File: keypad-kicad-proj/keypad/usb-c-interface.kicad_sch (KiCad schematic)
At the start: 23 parts, among them J2 USB4105-GF-A, Q1 BC817, Q2 BC817, U3 CP2102N-A01-GQFN24

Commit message: battery source
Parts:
- added C9: 1uF, symbol PutRocketLab_RCL:C_Small
- added SW13: SW_SPST, symbol Switch:SW_SPST
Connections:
- net GND: now also C9.2, SW13.1 (A)
- net RTS: now also C9.1, SW13.2 (B)
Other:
- note added: "Manual reset"
- moved on the sheet: C4, D18, D19, D20, D21, J2

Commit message: rest of the schematic
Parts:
- removed C9: 1uF, symbol PutRocketLab_RCL:C_Small
- removed SW13: SW_SPST, symbol Switch:SW_SPST
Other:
- note removed: "Manual reset"
- title: (none) -> Keypad board
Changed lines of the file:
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@@
 (kicad_sch (version 20230121) (generator eeschema)
   (paper "A4")
+  (title_block
+    (title "Keypad board")
+    (date "2023-11-15")
+    (rev "1.1")
+  )
   (junction (at 214.63 118.11) (diameter 0) (color 0 0 0 0)
   )
@@
   (junction (at 77.47 55.88) (diameter 0) (color 0 0 0 0)
   )
-  (junction (at 257.81 142.24) (diameter 0) (color 0 0 0 0)
-  )
   (junction (at 90.17 154.94) (diameter 0) (color 0 0 0 0)
   )
@@
   )
   (junction (at 165.1 111.76) (diameter 0) (color 0 0 0 0)
-  )
-  (junction (at 265.43 133.35) (diameter 0) (color 0 0 0 0)
   )
   (junction (at 78.74 154.94) (diameter 0) (color 0 0 0 0)
@@
     (stroke (width 0) (type default))
   )
-  (wire (pts (xy 257.81 142.24) (xy 265.43 142.24))
-    (stroke (width 0) (type default))
-  )
   (wire (pts (xy 102.87 45.72) (xy 109.22 45.72))
     (stroke (width 0) (type default))
@@
     (stroke (width 0) (type default))
   )
-  (wire (pts (xy 265.43 133.35) (xy 265.43 135.89))
-    (stroke (width 0) (type default))
-  )
   (wire (pts (xy 267.97 77.47) (xy 262.89 77.47))
     (stroke (width 0) (type default))
@@
     (stroke (width 0) (type default))
   )
-  (wire (pts (xy 250.19 142.24) (xy 257.81 142.24))
-    (stroke (width 0) (type default))
-  )
   (wire (pts (xy 76.2 185.42) (xy 76.2 152.4))
     (stroke (width 0) (type default))
@@
     (stroke (width 0) (type default))
   )
-  (wire (pts (xy 262.89 133.35) (xy 265.43 133.35))
-    (stroke (width 0) (type default))
-  )
   (wire (pts (xy 72.39 175.26) (xy 72.39 176.53))
     (stroke (width 0) (type default))
@@
     (stroke (width 0) (type default))
   )
-  (wire (pts (xy 257.81 144.78) (xy 257.81 142.24))
-    (stroke (width 0) (type default))
-  )
   (wire (pts (xy 170.18 101.6) (xy 198.12 101.6))
     (stroke (width 0) (type default))
@@
     (stroke (width 0) (type default))
   )
-  (wire (pts (xy 252.73 133.35) (xy 250.19 133.35))
-    (stroke (width 0) (type default))
-  )
   (wire (pts (xy 26.67 157.48) (xy 29.21 157.48))
     (stroke (width 0) (type default))
@@
     (stroke (width 0) (type default))
   )
-  (wire (pts (xy 265.43 133.35) (xy 267.97 133.35))
-    (stroke (width 0) (type default))
-  )
   (wire (pts (xy 196.85 106.68) (xy 198.12 106.68))
     (stroke (width 0) (type default))
@@
     (stroke (width 0) (type default))
   )
-  (wire (pts (xy 265.43 142.24) (xy 265.43 140.97))
-    (stroke (width 0) (type default))
-  )
   (wire (pts (xy 139.7 160.02) (xy 135.89 160.02))
     (stroke (width 0) (type default))
   )
   (wire (pts (xy 77.47 48.26) (xy 74.93 48.26))
-    (stroke (width 0) (type default))
-  )
-  (wire (pts (xy 250.19 133.35) (xy 250.19 142.24))
     (stroke (width 0) (type default))
   )
@@
   (text "USB-C (UART)" (at 36.83 22.86 0)
     (effects (font (size 3 3) (thickness 0.6) bold) (justify left bottom))
-  )
-  (text "Manual reset" (at 250.19 123.19 0)
-    (effects (font (size 1.5 1.5) (thickness 0.6) bold) (justify left bottom))
-  )
-  (global_label "RTS" (shape output) (at 267.97 133.35 0) (fields_autoplaced)
-    (effects (font (size 1.27 1.27)) (justify left))
-    (property "Intersheetrefs" "${INTERSHEET_REFS}" (at 274.4023 133.35 0)
-      (effects (font (size 1.27 1.27)) (justify left) hide)
-    )
   )
   (global_label "UART_RX" (shape input) (at 229.87 86.36 0) (fields_autoplaced)
@@
     )
   )
-  (symbol (lib_id "PutRocketLab_RCL:C_Small") (at 265.43 138.43 0) (unit 1)
-    (in_bom yes) (on_board yes) (dnp no) (fields_autoplaced)
-    (property "Reference" "C9" (at 267.97 137.1663 0)
-      (effects (font (size 1.27 1.27)) (justify left))
-    )
-    (property "Value" "1uF" (at 267.97 139.7063 0)
-      (effects (font (size 1.27 1.27)) (justify left))
-    )
-    (property "Footprint" "" (at 265.43 138.43 0)
-      (effects (font (size 1.27 1.27)) hide)
-    )
-    (property "Datasheet" "~" (at 265.43 138.43 0)
-      (effects (font (size 1.27 1.27)) hide)
-    )
-    (pin "1")
-    (pin "2")
-    (instances
-      (project "keypad"
-        (path "/26078c39-1d91-4154-8719-da74cb453e74/8c59234c-4b92-497c-9a92-28fee1185425"
-          (reference "C9") (unit 1)
-        )
-      )
-    )
-  )
   (symbol (lib_id "PutRocketLab_RCL:C_Small") (at 139.7 154.94 0) (unit 1)
     (in_bom yes) (on_board yes) (dnp no) (fields_autoplaced)
@@
         (path "/26078c39-1d91-4154-8719-da74cb453e74/8c59234c-4b92-497c-9a92-28fee1185425"
           (reference "R8") (unit 1)
-        )
-      )
-    )
-  )
-  (symbol (lib_id "Switch:SW_SPST") (at 257.81 133.35 0) (unit 1)
-    (in_bom yes) (on_board yes) (dnp no) (fields_autoplaced)
-    (property "Reference" "SW13" (at 257.81 127 0)
-      (effects (font (size 1.27 1.27)))
-    )
-    (property "Value" "SW_SPST" (at 257.81 129.54 0)
-      (effects (font (size 1.27 1.27)))
-    )
-    (property "Footprint" "" (at 257.81 133.35 0)
-      (effects (font (size 1.27 1.27)) hide)
-    )
-    (property "Datasheet" "~" (at 257.81 133.35 0)
-      (effects (font (size 1.27 1.27)) hide)
-    )
-    (pin "1")
-    (pin "2")
-    (instances
-      (project "keypad"
-        (path "/26078c39-1d91-4154-8719-da74cb453e74/4b0bf287-ff22-46d2-9a21-8f5bc40c75ad"
-          (reference "SW13") (unit 1)
-        )
-        (path "/26078c39-1d91-4154-8719-da74cb453e74/8c59234c-4b92-497c-9a92-28fee1185425"
-          (reference "SW25") (unit 1)
         )
       )
@@
         )
       )
-    )
-  )
-  (symbol (lib_id "PUT_RocketLab_power:GND") (at 257.81 144.78 0) (unit 1)
-    (in_bom yes) (on_board yes) (dnp no) (fields_autoplaced)
-    (property "Reference" "#PWR014" (at 257.81 151.13 0)
-      (effects (font (size 1.27 1.27)) hide)
-    )
-    (property "Value" "GND" (at 257.81 149.86 0)
-      (effects (font (size 1.27 1.27)))
-    )
-    (property "Footprint" "" (at 257.81 144.78 0)
-      (effects (font (size 1.27 1.27)) hide)
-    )
-    (property "Datasheet" "" (at 257.81 144.78 0)
-      (effects (font (size 1.27 1.27)) hide)
-    )
-    (pin "1")
-    (instances
-      (project "keypad"
-        (path "/26078c39-1d91-4154-8719-da74cb453e74"
-          (reference "#PWR014") (unit 1)
-        )
-        (path "/26078c39-1d91-4154-8719-da74cb453e74/8c59234c-4b92-497c-9a92-28fee1185425"
-          (reference "#PWR042") (unit 1)
-        )
-      )

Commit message: footprints
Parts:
- C3, C4, C6: footprint (none) -> Capacitor_SMD:C_0402_1005Metric
- C5: footprint (none) -> Capacitor_SMD:C_0603_1608Metric
- R10, R11, R7, R8, R9: footprint (none) -> Resistor_SMD:R_0603_1608Metric
- R5: footprint (none) -> Resistor_SMD:R_0402_1005Metric
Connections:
- net +3V3: now also U3.5 (VIO)
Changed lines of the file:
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@@
   (junction (at 245.11 93.98) (diameter 0) (color 0 0 0 0)
+  )
+  (junction (at 210.82 69.85) (diameter 0) (color 0 0 0 0)
   )
   (junction (at 170.18 101.6) (diameter 0) (color 0 0 0 0)
@@
     (stroke (width 0) (type default))
   )
+  (wire (pts (xy 213.36 69.85) (xy 210.82 69.85))
+    (stroke (width 0) (type default))
+  )
   (wire (pts (xy 26.67 73.66) (xy 81.28 73.66))
     (stroke (width 0) (type default))
@@
   )
   (wire (pts (xy 31.75 45.72) (xy 34.29 45.72))
+    (stroke (width 0) (type default))
+  )
+  (wire (pts (xy 213.36 71.12) (xy 213.36 69.85))
     (stroke (width 0) (type default))
   )
@@
       (effects (font (size 1.27 1.27)) (justify left))
     )
-    (property "Footprint" "" (at 64.77 99.06 0)
+    (property "Footprint" "Capacitor_SMD:C_0402_1005Metric" (at 64.77 99.06 0)
       (effects (font (size 1.27 1.27)) hide)
     )
@@
       (effects (font (size 1.27 1.27)) (justify right))
     )
-    (property "Footprint" "" (at 160.02 96.52 0)
+    (property "Footprint" "Resistor_SMD:R_0402_1005Metric" (at 160.02 96.52 0)
       (effects (font (size 1.27 1.27)) hide)
     )
@@
       (effects (font (size 1.27 1.27)) (justify left))
     )
-    (property "Footprint" "" (at 170.18 106.68 0)
+    (property "Footprint" "Capacitor_SMD:C_0603_1608Metric" (at 170.18 106.68 0)
       (effects (font (size 1.27 1.27)) hide)
     )
@@
       (effects (font (size 1.27 1.27)) (justify left))
     )
-    (property "Footprint" "" (at 139.7 154.94 0)
+    (property "Footprint" "Capacitor_SMD:C_0402_1005Metric" (at 139.7 154.94 0)
       (effects (font (size 1.27 1.27)) hide)
     )
@@
       (effects (font (size 1.27 1.27)) (justify left))
     )
-    (property "Footprint" "" (at 191.77 88.9 0)
+    (property "Footprint" "Resistor_SMD:R_0603_1608Metric" (at 191.77 88.9 0)
       (effects (font (size 1.27 1.27)) hide)
     )
@@
       (effects (font (size 1.27 1.27)) (justify right))
     )
-    (property "Footprint" "" (at 160.02 106.68 0)
+    (property "Footprint" "Resistor_SMD:R_0603_1608Metric" (at 160.02 106.68 0)
       (effects (font (size 1.27 1.27)) hide)
     )
@@
       (effects (font (size 1.27 1.27)))
     )
-    (property "Footprint" "" (at 191.77 69.85 0)
+    (property "Footprint" "Capacitor_SMD:C_0402_1005Metric" (at 191.77 69.85 0)
       (effects (font (size 1.27 1.27)) hide)
     )
@@
       (effects (font (size 1.27 1.27)) (justify right))
     )
-    (property "Footprint" "" (at 191.77 78.74 0)
+    (property "Footprint" "Resistor_SMD:R_0603_1608Metric" (at 191.77 78.74 0)
       (effects (font (size 1.27 1.27)) hide)
     )
@@
       (effects (font (size 1.27 1.27)) (justify right))
     )
-    (property "Footprint" "" (at 251.46 83.82 0)
+    (property "Footprint" "Resistor_SMD:R_0603_1608Metric" (at 251.46 83.82 0)
       (effects (font (size 1.27 1.27)) hide)
     )
@@
       (effects (font (size 1.27 1.27)) (justify right))
     )
-    (property "Footprint" "" (at 251.46 100.33 0)
-      (effects (font (size 1.27 1.27)) hide)
-    )
+    (property "Footprint" "Resistor_SMD:R_0603_1608Metric" (at 251.46 100.33 0)
+      (effects (font (size 1.27 1.27)) hide)
+    )

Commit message: add all footprints & move libs to project specific
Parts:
- D17, D18: footprint (none) -> Diode_SMD:D_2114_3652Metric
- J2: footprint PUTRocketLab_other:GCT_USB4105-GF-A -> PUT_RocketLab_other:GCT_USB4105-GF-A
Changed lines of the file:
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@@
       (effects (font (size 1.27 1.27)))
     )
-    (property "Footprint" "PUTRocketLab_other:GCT_USB4105-GF-A" (at 54.61 45.72 0)
+    (property "Footprint" "PUT_RocketLab_other:GCT_USB4105-GF-A" (at 54.61 45.72 0)
       (effects (font (size 1.27 1.27)) (justify left bottom) hide)
     )
@@
       (effects (font (size 1.27 1.27)))
     )
-    (property "Footprint" "" (at 125.73 147.32 0)
-      (effects (font (size 1.27 1.27)) hide)
-    )
-    (property "Datasheet" "~" (at 125.73 147.32 0)
+    (property "Footprint" "Diode_SMD:D_2114_3652Metric" (at 125.73 147.32 0)
+      (effects (font (size 1.27 1.27)) hide)
+    )
+    (property "Datasheet" "https://www.mouser.pl/datasheet/2/80/CDBA240LR_HF_Thru514819__CDBA2200LR_HF_RevB-2505020.pdf" (at 125.73 147.32 0)
       (effects (font (size 1.27 1.27)) hide)
     )
@@
       (effects (font (size 1.27 1.27)))
     )
-    (property "Footprint" "PUTRocketLab_other:GCT_USB4105-GF-A" (at 49.53 157.48 0)
+    (property "Footprint" "PUT_RocketLab_other:GCT_USB4105-GF-A" (at 49.53 157.48 0)
       (effects (font (size 1.27 1.27)) (justify left bottom) hide)
     )
@@
       (effects (font (size 1.27 1.27)))
     )
-    (property "Footprint" "" (at 50.8 91.44 0)
-      (effects (font (size 1.27 1.27)) hide)
-    )
-    (property "Datasheet" "~" (at 50.8 91.44 0)
-      (effects (font (size 1.27 1.27)) hide)
-    )
+    (property "Footprint" "Diode_SMD:D_2114_3652Metric" (at 50.8 91.44 0)
+      (effects (font (size 1.27 1.27)) hide)
+    )
+    (property "Datasheet" "https://www.mouser.pl/datasheet/2/80/CDBA240LR_HF_Thru514819__CDBA2200LR_HF_RevB-2505020.pdf" (at 50.8 91.44 0)
+      (effects (font (size 1.27 1.27)) hide)
+    )

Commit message: main layout
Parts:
- C3, C4, C6: footprint Capacitor_SMD:C_0402_1005Metric -> Capacitor_SMD:C_0603_1608Metric
- R5: footprint Resistor_SMD:R_0402_1005Metric -> Resistor_SMD:R_0603_1608Metric
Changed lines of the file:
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@@
       (effects (font (size 1.27 1.27)) (justify left))
     )
-    (property "Footprint" "Capacitor_SMD:C_0402_1005Metric" (at 64.77 99.06 0)
+    (property "Footprint" "Capacitor_SMD:C_0603_1608Metric" (at 64.77 99.06 0)
       (effects (font (size 1.27 1.27)) hide)
     )
@@
       (effects (font (size 1.27 1.27)) (justify right))
     )
-    (property "Footprint" "Resistor_SMD:R_0402_1005Metric" (at 160.02 96.52 0)
+    (property "Footprint" "Resistor_SMD:R_0603_1608Metric" (at 160.02 96.52 0)
       (effects (font (size 1.27 1.27)) hide)
     )
@@
       (effects (font (size 1.27 1.27)) (justify left))
     )
-    (property "Footprint" "Capacitor_SMD:C_0402_1005Metric" (at 139.7 154.94 0)
+    (property "Footprint" "Capacitor_SMD:C_0603_1608Metric" (at 139.7 154.94 0)
       (effects (font (size 1.27 1.27)) hide)
     )
@@
       (effects (font (size 1.27 1.27)))
     )
-    (property "Footprint" "Capacitor_SMD:C_0402_1005Metric" (at 191.77 69.85 0)
-      (effects (font (size 1.27 1.27)) hide)
-    )
+    (property "Footprint" "Capacitor_SMD:C_0603_1608Metric" (at 191.77 69.85 0)
+      (effects (font (size 1.27 1.27)) hide)
+    )

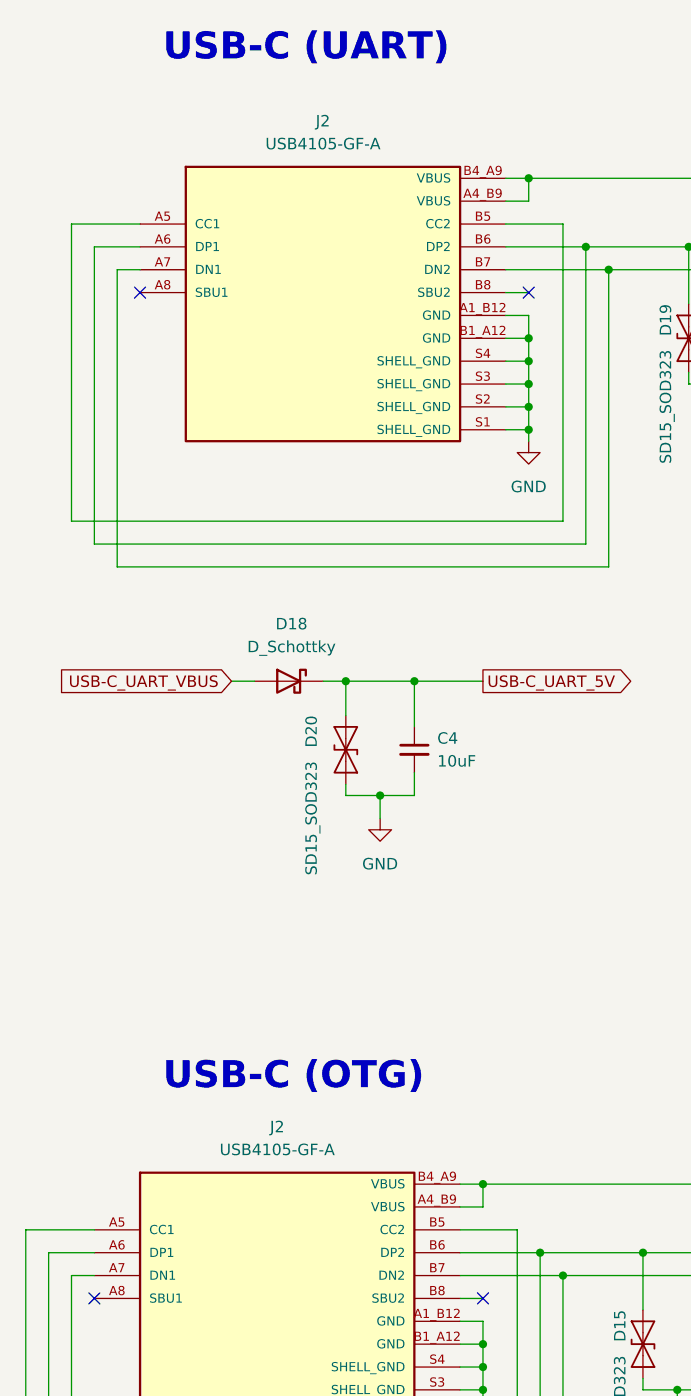
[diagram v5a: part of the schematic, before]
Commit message: assigned different pins so it's easier for the layout
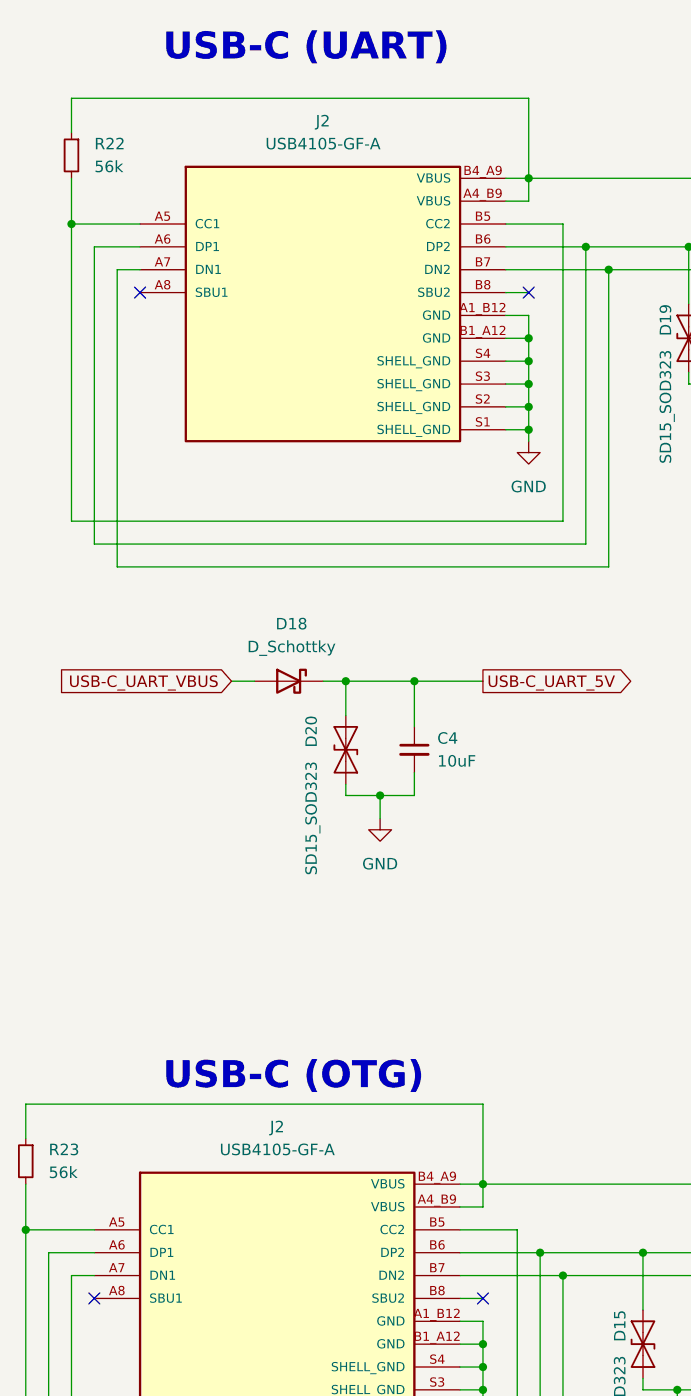
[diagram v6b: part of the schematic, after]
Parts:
- added R22, R23: 56k, Capacitor_SMD:C_0805_2012Metric, symbol PutRocketLab_RCL:R_Small
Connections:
- net USB-C_UART_VBUS: now also R22.1
- net at J2.A5 (CC1), J2.B5 (CC2): now also R22.2
- net at D17.2 (A), J2.A4_B9 (VBUS), J2.B4_A9 (VBUS): now also R23.1
- net at J2.A5 (CC1), J2.B5 (CC2): now also R23.2
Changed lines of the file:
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@@
   (junction (at 60.96 104.14) (diameter 0) (color 0 0 0 0)
   )
+  (junction (at 26.67 40.64) (diameter 0) (color 0 0 0 0)
+  )
   (junction (at 57.15 91.44) (diameter 0) (color 0 0 0 0)
   )
@@
   )
   (junction (at 72.39 167.64) (diameter 0) (color 0 0 0 0)
+  )
+  (junction (at 21.59 152.4) (diameter 0) (color 0 0 0 0)
   )
   (junction (at 77.47 63.5) (diameter 0) (color 0 0 0 0)
@@
     (stroke (width 0) (type default))
   )
+  (wire (pts (xy 21.59 147.32) (xy 21.59 152.4))
+    (stroke (width 0) (type default))
+  )
   (wire (pts (xy 26.67 190.5) (xy 26.67 157.48))
     (stroke (width 0) (type default))
@@
     (stroke (width 0) (type default))
   )
+  (wire (pts (xy 26.67 35.56) (xy 26.67 40.64))
+    (stroke (width 0) (type default))
+  )
+  (wire (pts (xy 77.47 26.67) (xy 77.47 35.56))
+    (stroke (width 0) (type default))
+  )
   (wire (pts (xy 60.96 104.14) (xy 57.15 104.14))
     (stroke (width 0) (type default))
@@
     (stroke (width 0) (type default))
   )
+  (wire (pts (xy 21.59 142.24) (xy 21.59 138.43))
+    (stroke (width 0) (type default))
+  )
+  (wire (pts (xy 21.59 138.43) (xy 72.39 138.43))
+    (stroke (width 0) (type default))
+  )
   (wire (pts (xy 245.11 100.33) (xy 248.92 100.33))
     (stroke (width 0) (type default))
@@
     (stroke (width 0) (type default))
   )
+  (wire (pts (xy 26.67 26.67) (xy 77.47 26.67))
+    (stroke (width 0) (type default))
+  )
   (wire (pts (xy 228.6 83.82) (xy 246.38 83.82))
     (stroke (width 0) (type default))
@@
     (stroke (width 0) (type default))
   )
+  (wire (pts (xy 26.67 30.48) (xy 26.67 26.67))
+    (stroke (width 0) (type default))
+  )
   (wire (pts (xy 64.77 101.6) (xy 64.77 104.14))
     (stroke (width 0) (type default))
@@
   )
   (wire (pts (xy 246.38 83.82) (xy 248.92 83.82))
+    (stroke (width 0) (type default))
+  )
+  (wire (pts (xy 72.39 138.43) (xy 72.39 147.32))
     (stroke (width 0) (type default))
   )
@@
     )
   )
+  (symbol (lib_id "PutRocketLab_RCL:R_Small") (at 26.67 33.02 0) (mirror y) (unit 1)
+    (in_bom yes) (on_board yes) (dnp no)
+    (property "Reference" "R22" (at 29.21 31.75 0)
+      (effects (font (size 1.27 1.27)) (justify right))
+    )
+    (property "Value" "56k" (at 29.21 34.29 0)
+      (effects (font (size 1.27 1.27)) (justify right))
+    )
+    (property "Footprint" "Capacitor_SMD:C_0805_2012Metric" (at 26.67 33.02 0)
+      (effects (font (size 1.27 1.27)) hide)
+    )
+    (property "Datasheet" "~" (at 26.67 33.02 0)
+      (effects (font (size 1.27 1.27)) hide)
+    )
+    (pin "1")
+    (pin "2")
+    (instances
+      (project "keypad"
+        (path "/26078c39-1d91-4154-8719-da74cb453e74/8c59234c-4b92-497c-9a92-28fee1185425"
+          (reference "R22") (unit 1)
+        )
+      )
+    )
+  )
   (symbol (lib_id "PutRocketLab_RCL:C_Small") (at 170.18 106.68 0) (unit 1)
     (in_bom yes) (on_board yes) (dnp no) (fields_autoplaced)
@@
         )
       )
+    )
+  )
+  (symbol (lib_id "PutRocketLab_RCL:R_Small") (at 21.59 144.78 0) (mirror y) (unit 1)
+    (in_bom yes) (on_board yes) (dnp no)
+    (property "Reference" "R23" (at 24.13 143.51 0)
+      (effects (font (size 1.27 1.27)) (justify right))
+    )
+    (property "Value" "56k" (at 24.13 146.05 0)
+      (effects (font (size 1.27 1.27)) (justify right))
+    )
+    (property "Footprint" "Capacitor_SMD:C_0805_2012Metric" (at 21.59 144.78 0)
+      (effects (font (size 1.27 1.27)) hide)
+    )
+    (property "Datasheet" "~" (at 21.59 144.78 0)
+      (effects (font (size 1.27 1.27)) hide)
+    )
+    (pin "1")
+    (pin "2")
+    (instances
+      (project "keypad"
+        (path "/26078c39-1d91-4154-8719-da74cb453e74/8c59234c-4b92-497c-9a92-28fee1185425"
+          (reference "R23") (unit 1)
+        )
+      )
